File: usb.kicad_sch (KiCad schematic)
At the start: 9 parts, among them J2 USB_C_Receptacle_USB2.0_16P, J3 Conn_01x05_Pin, U2 TPS25750DRJKR

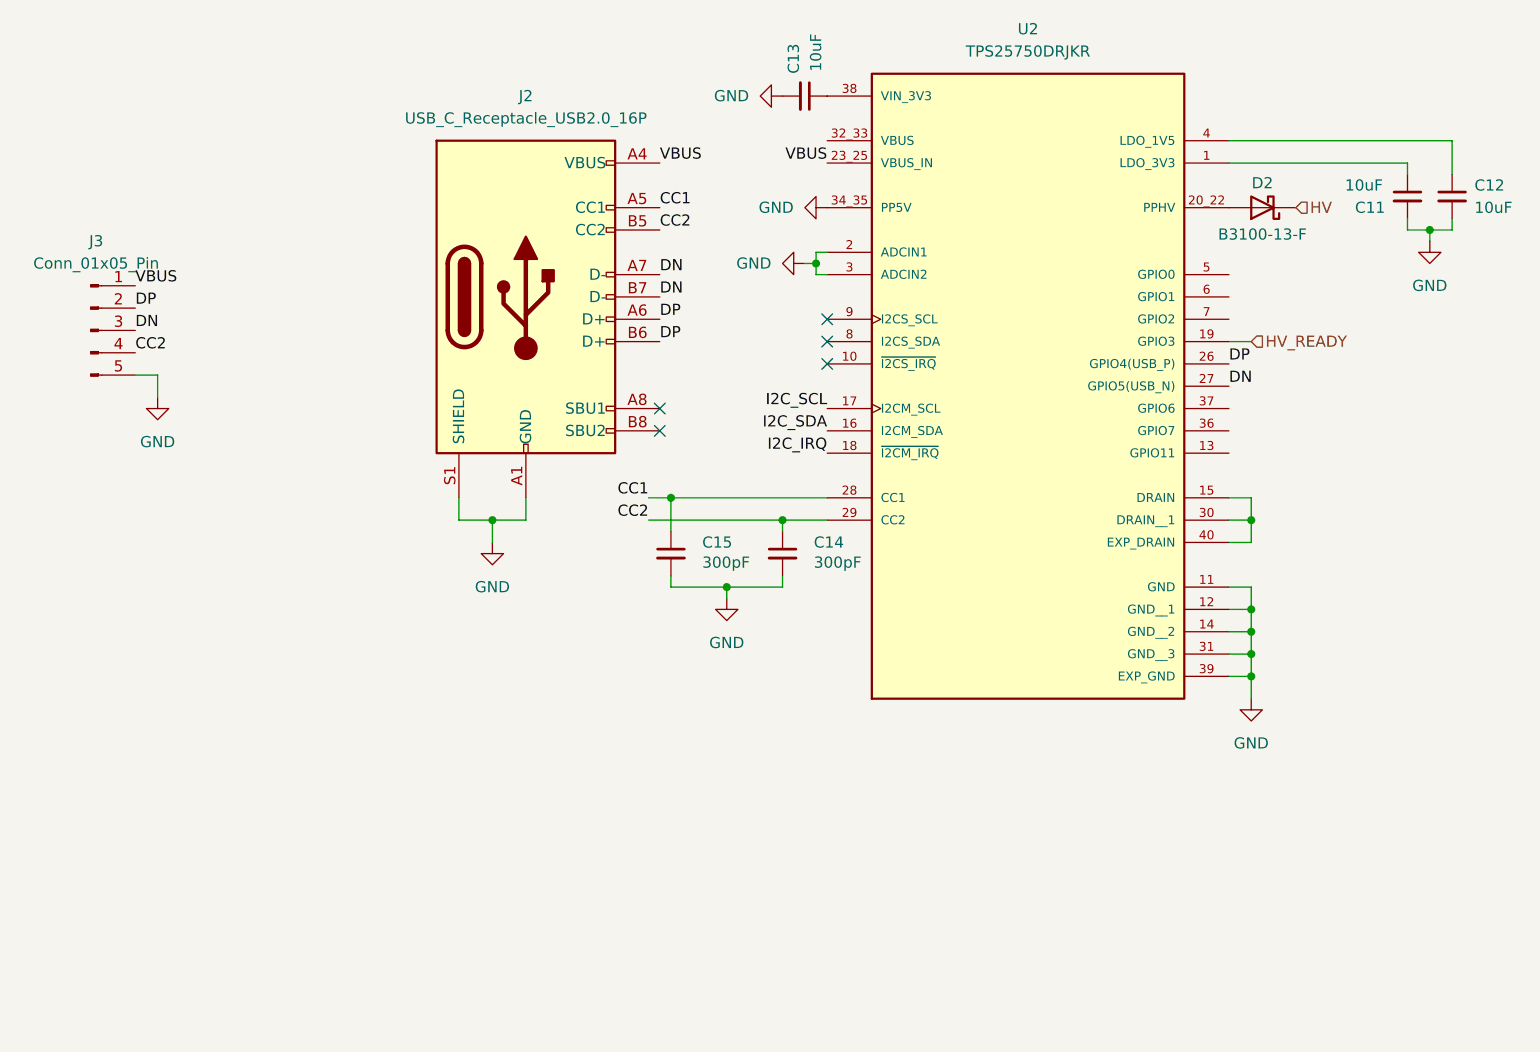
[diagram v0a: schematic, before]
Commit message: feat: fully routed USB-PD, new lower profile inductor
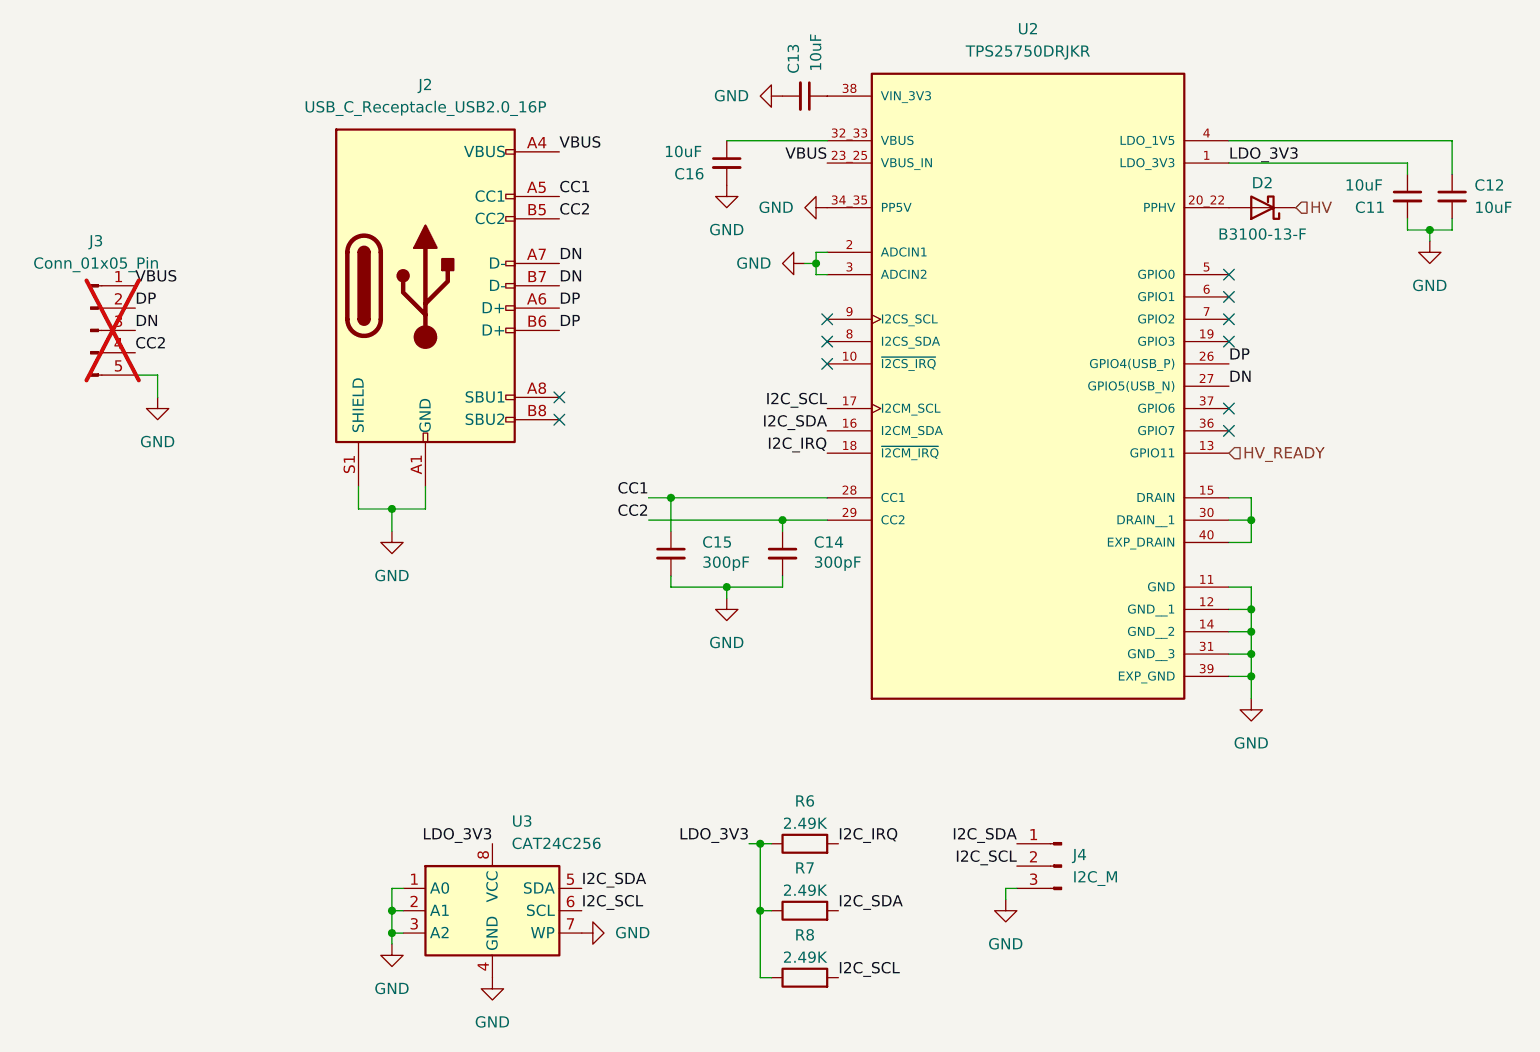
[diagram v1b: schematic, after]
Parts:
- added C16: 10uF, Capacitor_SMD:C_0402_1005Metric, symbol Device:C_Small
- added J4: I2C_M, Connector_PinHeader_2.54mm:PinHeader_1x03_P2.54mm_Vertical, symbol Connector:Conn_01x03_Pin
- added R6, R7, R8: 2.49K, Resistor_SMD:R_0603_1608Metric, symbol Device:R
- added U3: CAT24C256, Package_SO:SOIC-8_3.9x4.9mm_P1.27mm, symbol Memory_EEPROM:CAT24C256
- J3: now not fitted; now left out of the parts list
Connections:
- net GND: now also C16.2, J4.3 (Pin_3), U3.1 (A0), U3.2 (A1), U3.3 (A2), U3.4 (GND), U3.7 (WP)
- net HV_READY: now also U2.13 (GPIO11); no longer U2.19 (GPIO3)
- net I2C_IRQ: now also R6.2
- net I2C_SCL: now also J4.2 (Pin_2), R8.2, U3.6 (SCL)
- net I2C_SDA: now also J4.1 (Pin_1), R7.2, U3.5 (SDA)
- net LDO_3V3: now reaches C11.1, U2.1 (LDO_3V3)
- net LDO_3V3: now also R6.1, R7.1, R8.1, U3.8 (VCC)
- net at U2.32_33 (VBUS): now also C16.1
- no-connect marks 5 -> 11
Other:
- moved on the sheet: J2

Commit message: patch: final trace cleaups/parameter updates
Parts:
- C11, C12, C13, C16: Part C525328 -> C2992625
- U3: Part (none) -> C79987
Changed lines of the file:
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@@
 			)
 		)
-		(property "Part" "C525328"
+		(property "Part" "C2992625"
 			(at 205.74 81.28 0)
 			(effects
@@
 			)
 		)
-		(property "Part" "C525328"
+		(property "Part" "C2992625"
 			(at 210.82 81.28 0)
 			(effects
@@
 			)
 		)
-		(property "Part" "C525328"
+		(property "Part" "C2992625"
 			(at 137.16 69.85 0)
 			(effects
@@
 			)
 		)
-		(property "Part" "C525328"
+		(property "Part" "C2992625"
 			(at 128.27 77.47 0)
 			(effects
@@
 			(at 101.6 162.56 0)
 			(effects
+				(font
+					(size 1.27 1.27)
+				)
+				(hide yes)
+			)
+		)
+		(property "Part" "C79987"
+			(at 101.6 162.56 0)
+			(effects
